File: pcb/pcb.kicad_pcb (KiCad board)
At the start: 2 copper layers, 105 x 45.1 mm, 12 parts, among them U1 ICM7555xP

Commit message: fix some errors
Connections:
- ON1 pad 2: 3Volt -> Net-(U1-TR)
- R3 pad 2: 3Volt -> Net-(U1-TR)
- U1 pad 2: 3Volt -> Net-(U1-TR)
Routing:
- net 3Volt: track 116.5 -> 89.9 mm
- net Net-(U1-TR): track 0.00 -> 17.9 mm

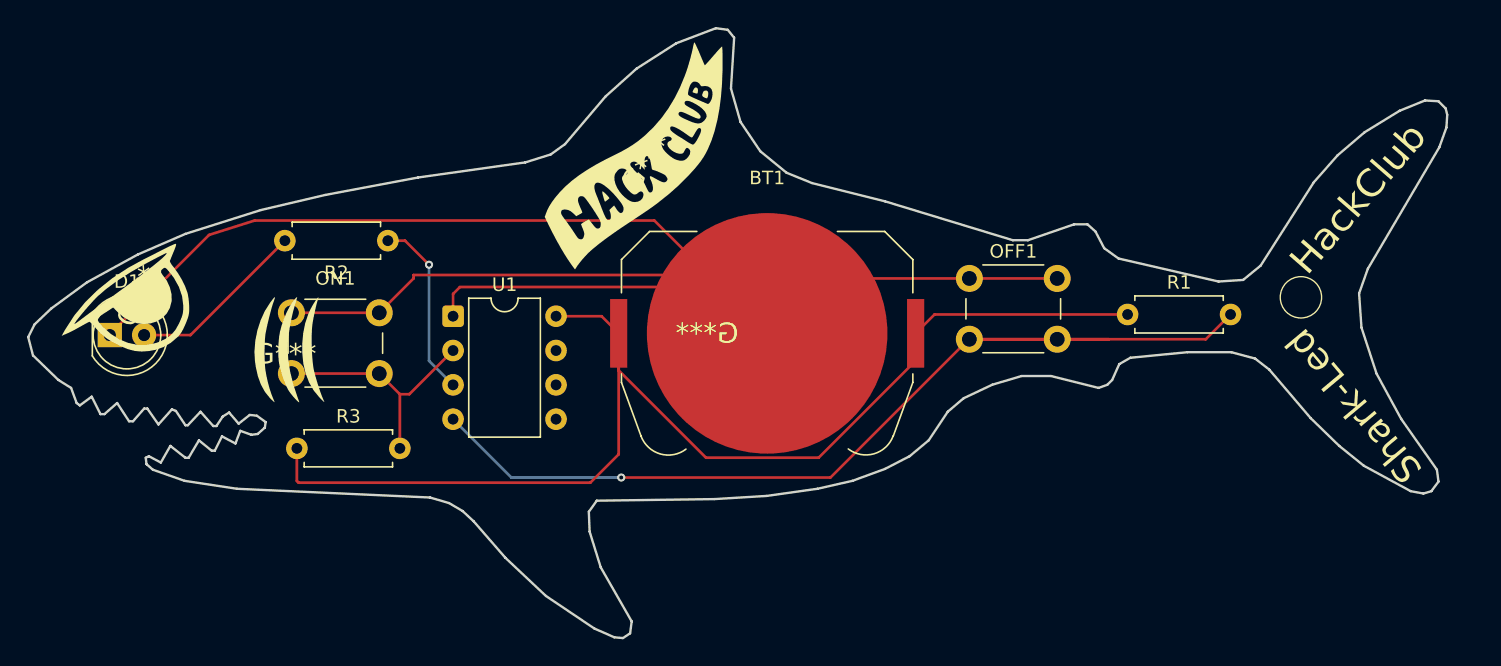
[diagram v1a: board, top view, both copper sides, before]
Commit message: add some components
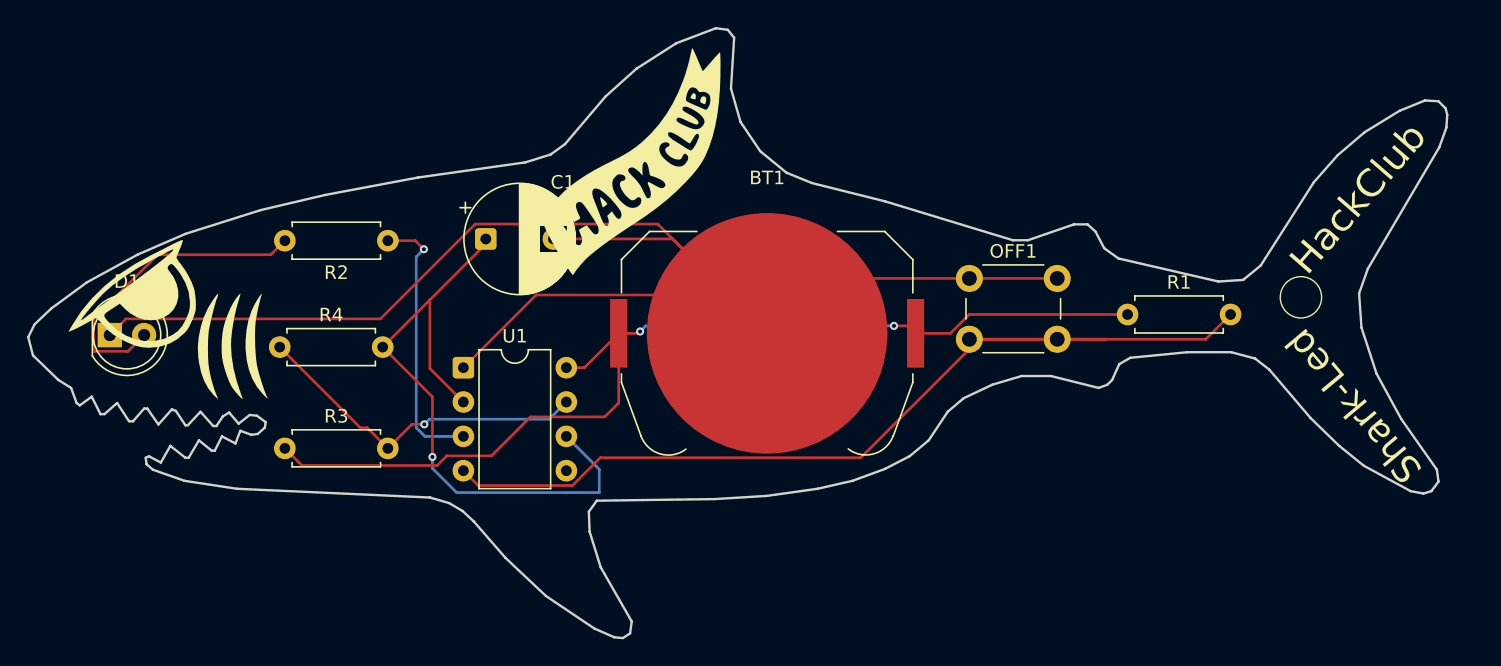
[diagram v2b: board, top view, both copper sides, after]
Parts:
- removed ON1: SW_Push, Button_Switch_THT:SW_PUSH_6mm
- added C1: 10µF, Capacitor_THT:CP_Radial_D8.0mm_P5.00mm, F.Cu at (139.6, 95.8)
- added R4: 4.7k, Resistor_THT:R_Axial_DIN0207_L6.3mm_D2.5mm_P7.62mm_Horizontal, F.Cu at (124.3, 103.8)
- R3: value 47k -> 4.7k
- moved G*** 4.20 mm to (120.5, 104.0)
- moved U1 3.89 mm to (137.9, 105.3)
- moved G*** 2.08 mm to (154.3, 101.5)
- moved R3 0.89 mm to (124.7, 111.3)
- moved G*** 0.57 mm to (114.3, 99.7)
- moved G*** 0.46 mm to (151.4, 90.6)
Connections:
- R3 pad 2: Net-(U1-TR) -> Net-(U1-DIS)
- U1 pad 2: Net-(U1-TR) -> Net-(U1-THR)
- U1 pad 6: unconnected-(U1-THR-Pad6) -> Net-(U1-THR)
- U1 pad 7: unconnected-(U1-DIS-Pad7) -> Net-(U1-DIS)
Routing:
- net Net-(U1-THR): track 0.00 -> 48.5 mm, vias 0 -> 1
- net Net-(U1-DIS): track 0.00 -> 25.7 mm, vias 0 -> 1
- net GND: track 143.3 -> 123.1 mm
- net Net-(U1-TR): track 17.9 -> 0.00 mm
- net 3Volt: track 89.9 -> 75.9 mm, vias 0 -> 2
- net Net-(D1-A): track 13.3 -> 23.2 mm
- net Net-(U1-Q): track 13.4 -> 20.1 mm
- net Net-(U1-R): track 74.6 -> 72.5 mm, vias 1 -> 0
